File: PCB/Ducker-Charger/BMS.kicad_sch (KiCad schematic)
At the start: 0 parts

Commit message: feat: started BMS configuration
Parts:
- added C15, C16, C17, C18, C_VDD, C_VDD1: 1u, symbol Device:C
- added Q5, Q6: NCE3080K, EasyEDA:TO-252-2_L6.6-W6.1-P4.57-LS9.9-TL-CW, symbol EasyEDA:NCE3080K
- added R10: 10m, symbol Device:R
- added R11, R12, R13, R14, R15: 50, symbol Device:R
- added R_VDD: 1k, symbol Device:R
- added TH2: Thermistor_NTC, symbol Device:Thermistor_NTC
- added U4: BQ7791500PWR, EasyEDA:TSSOP-24_L7.8-W4.4-P0.65-LS6.4-BL, symbol EasyEDA:BQ7791500PWR
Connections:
- new net AVDD: C_VDD1.2, U4.2 (AVDD)
- new net BATT_+: R_VDD.1
- new net BATT_-: U4.9 (VSS)
- new net BATT_SENS_B+: R11.1
- new net BATT_SENS_B-: C_VDD.2, C_VDD1.1, R15.1
- new net BATT_SENS_B1: R14.1
- new net BATT_SENS_B2: R13.1
- new net BATT_SENS_B3: R12.1
- new net GND: U4.23 (CTRC), U4.24 (CTRD)
- new net VC0: C18.2, R15.2, U4.8 (VC0)
- new net VC1: C17.2, C18.1, R14.2, U4.7 (VC1)
- new net VC2: C16.2, C17.1, R13.2, U4.6 (VC2)
- new net VC3: C15.2, C16.1, R12.2, U4.5 (VC3)
- new net VC4: C15.1, R11.2, U4.3 (VC5), U4.4 (VC4)
- new net VDD: C_VDD.1, R_VDD.2, U4.1 (VDD)
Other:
- note added: "I_BAL = V_CELLA / (2 * R)=4.2V/100R=42mA P=RxI^2=~ 88mW"
- note added: "NB: VC5 and VC4 are shorted in order to make it usable with the configuration we are working with: 4s3p"
- note added: "NB: resistor package 0805, 0.125W"
- note added: "ntc need to be revaluated; i'd like to have at least 2 ntcs for parallel, but pheraps the distance will not allow it. i'm looking for a Epoxy NTC Thermistor with wire leads, which could be the answer to our problems"
- note added: "shunt"

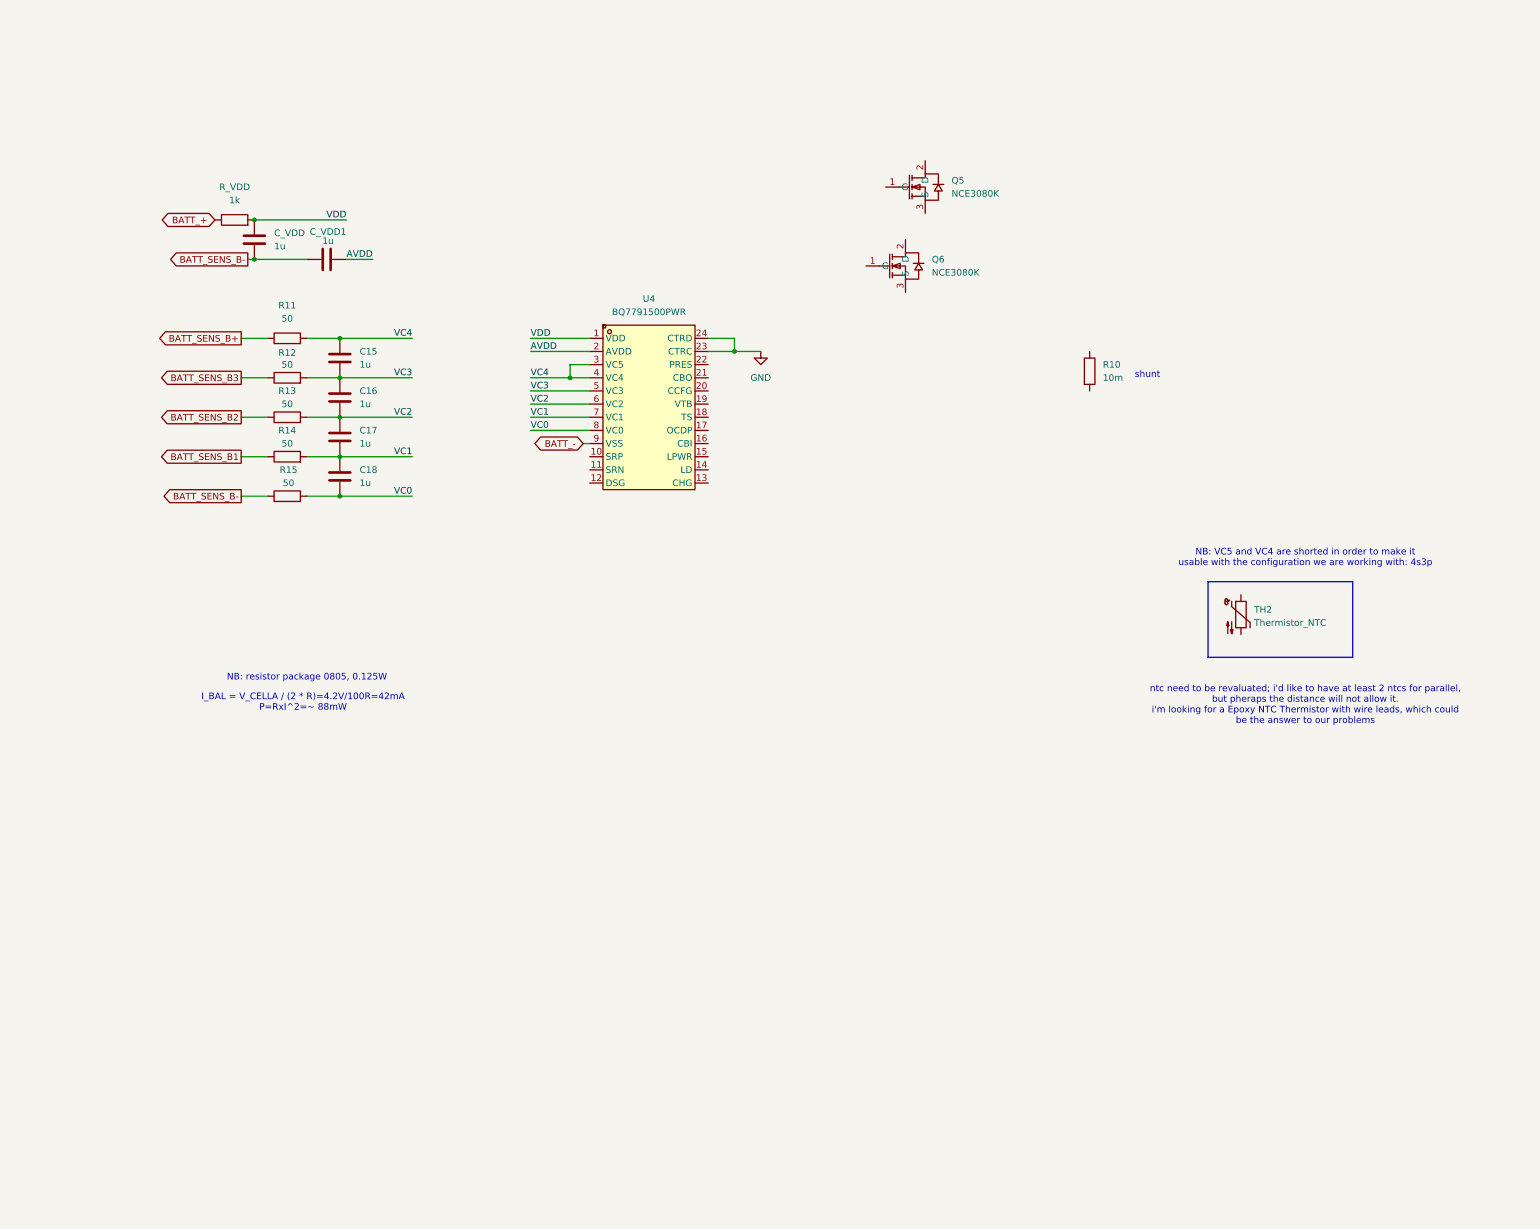
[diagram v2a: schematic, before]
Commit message: feat: started CHG and DSG in BMS
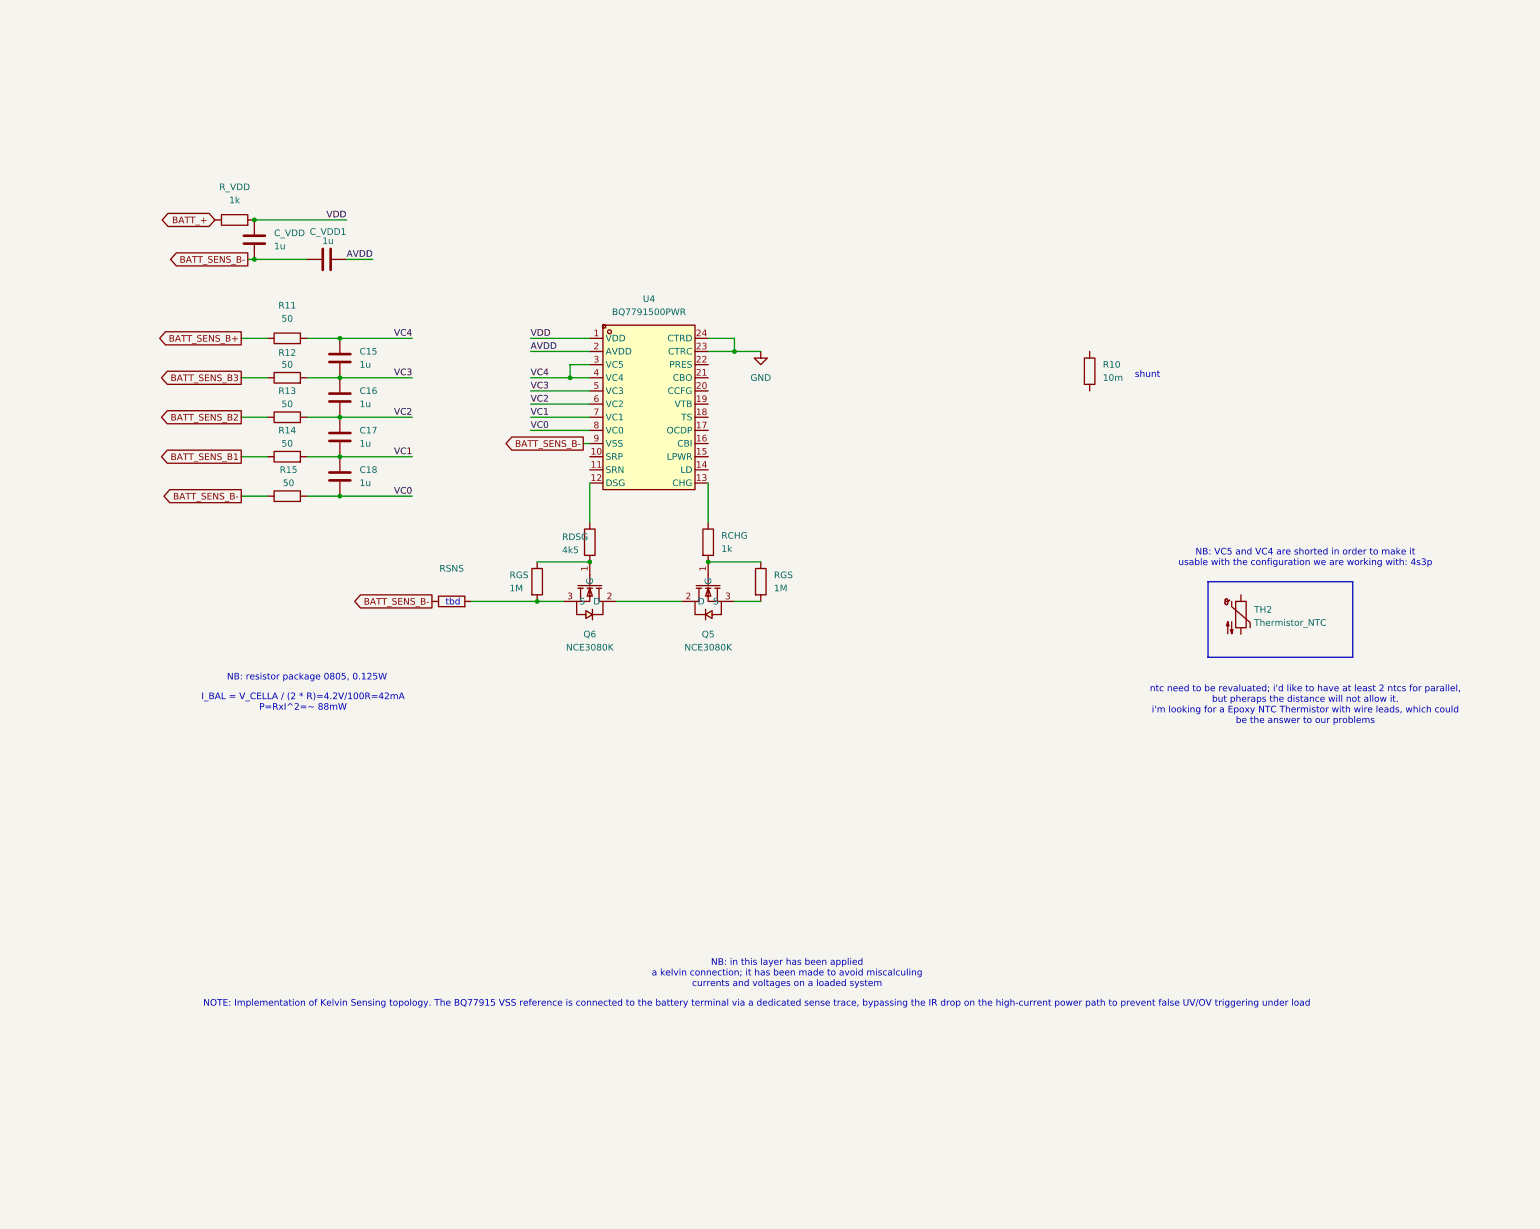
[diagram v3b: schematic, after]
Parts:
- added RCHG: 1k, symbol Device:R
- added RDSG: 4k5, symbol Device:R
- added RGS (x2): 1M, symbol Device:R
- added RSNS: ~, symbol Device:R
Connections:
- net BATT_- is gone; now on net BATT_SENS_B-: U4.9 (VSS)
- net BATT_SENS_B-: now also RSNS.1
- net at U4.12 (DSG): now also RDSG.1
- net at U4.13 (CHG): now also RCHG.1
- net at Q5.1 (G): now also RCHG.2, RGS.1
- net at Q5.2 (D): now also Q6.2 (D)
- net at Q5.3 (S): now also RGS.2
- net at Q6.1 (G): now also RDSG.2, RGS.1
- net at Q6.3 (S): now also RGS.2, RSNS.2
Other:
- note added: "NB: in this layer has been applied a kelvin connection; it has been made to avoid miscalculing currents and voltages on a loaded system"
- note added: "NOTE: Implementation of Kelvin Sensing topology. The BQ77915 VSS reference is connected to the battery terminal via a dedicated sense trace, bypassing the IR drop on the high-current power path to prevent false UV/OV triggering under load"
- note added: "tbd"
- moved on the sheet: Q5, Q6

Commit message: feat: implement basic BQ77915 protection circuit
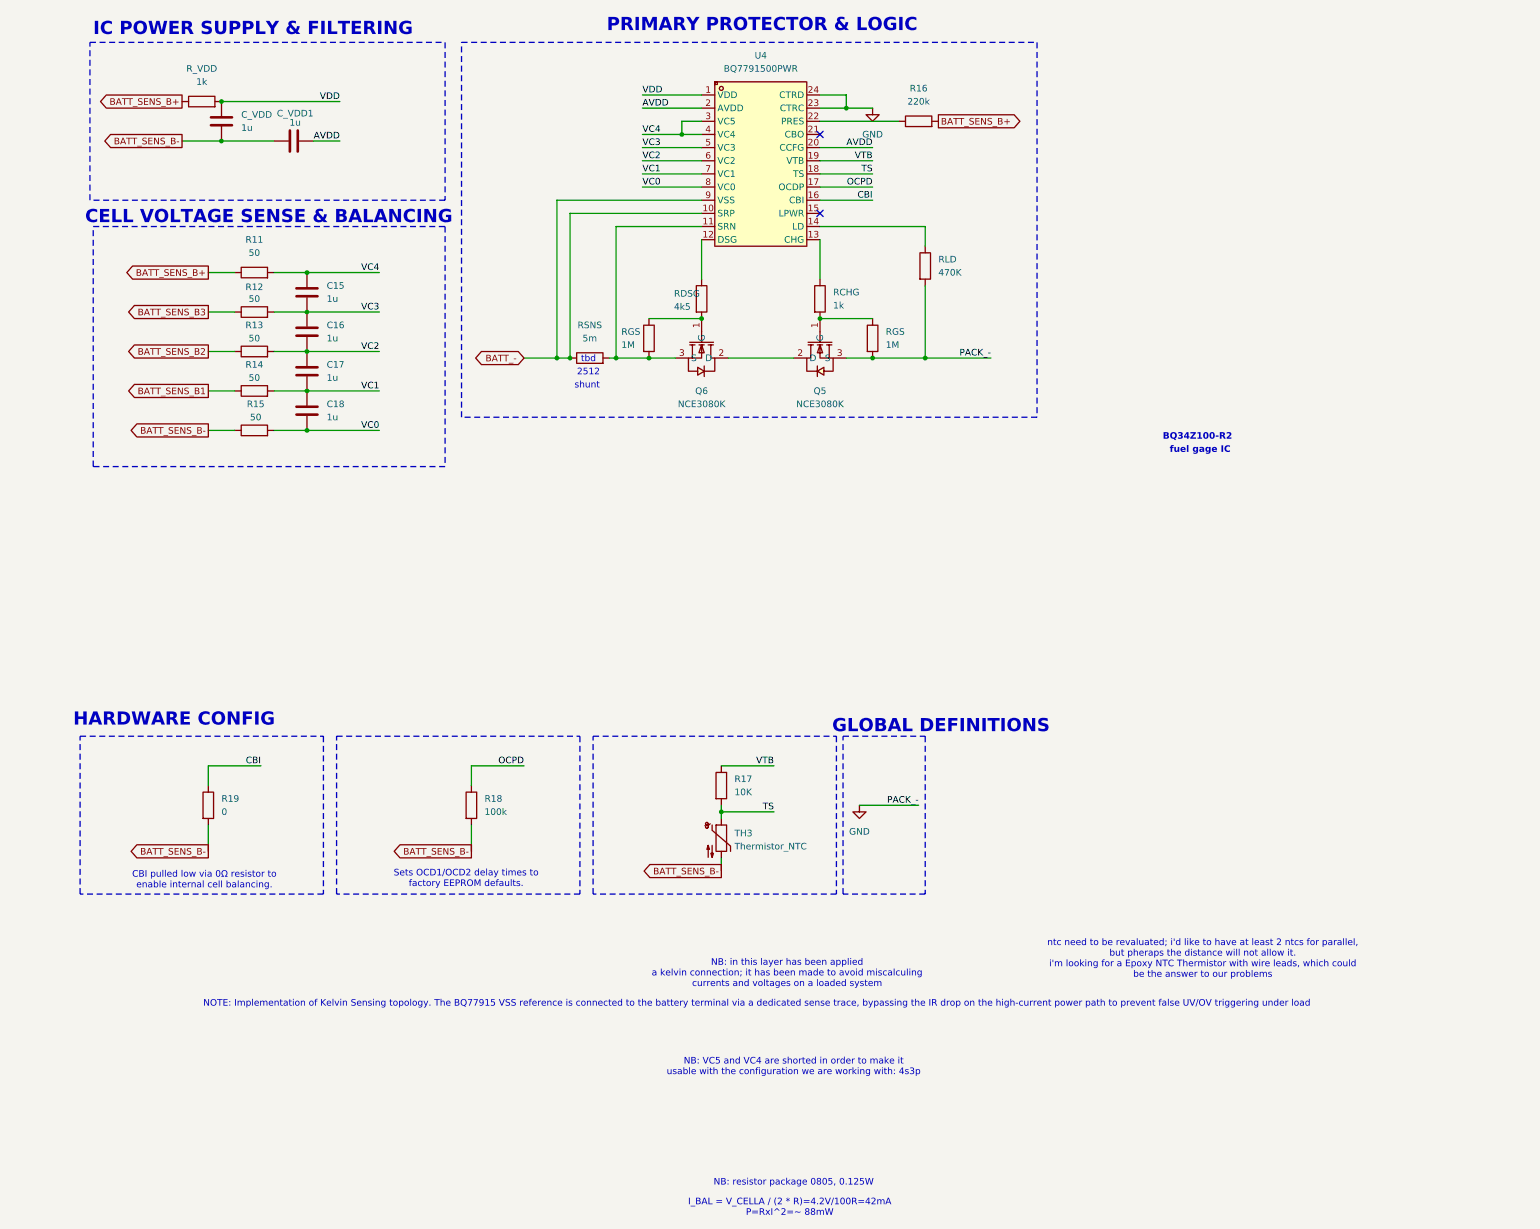
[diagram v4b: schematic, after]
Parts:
- removed R10: 10m, symbol Device:R
- removed TH2: Thermistor_NTC, symbol Device:Thermistor_NTC
- added R16: 220k, symbol Device:R
- added R17: 10K, symbol Device:R
- added R18: 100k, symbol Device:R
- added R19: 0, symbol Device:R
- added RLD: 470K, symbol Device:R
- added TH3: Thermistor_NTC, symbol Device:Thermistor_NTC
- RSNS: value ~ -> 5m; lcsc name (none) -> Milliohm HoJLR2512-3W-5mR-1%
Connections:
- net BATT_+ is gone; now on net BATT_SENS_B+: R_VDD.1
- net AVDD: now also U4.20 (CCFG)
- net BATT_SENS_B+: now also R16.2
- net BATT_SENS_B-: now also R18.2, R19.2, TH3.2; no longer RSNS.1, U4.9 (VSS)
- net GND: now also Q5.3 (S), RGS.2, RLD.2
- net at Q6.3 (S), RGS.2, RSNS.2: now also U4.11 (SRN)
- net BATT_-: now reaches U4.10 (SRP)
- net BATT_-: now also RSNS.1, U4.9 (VSS)
- net at U4.14 (LD): now also RLD.1
- net CBI: now reaches U4.16 (CBI)
- net CBI: now also R19.1
- net OCPD: now reaches U4.17 (OCDP)
- net OCPD: now also R18.1
- net TS: now reaches U4.18 (TS)
- net TS: now also R17.2, TH3.1
- net VTB: now reaches U4.19 (VTB)
- net VTB: now also R17.1
- net at U4.22 (PRES): now also R16.1
- no-connect marks 0 -> 2
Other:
- note added: "2512"
- note added: "BQ34Z100-R2"
- note added: "CBI pulled low via 0Ω resistor to enable internal cell balancing."
- note added: "CELL VOLTAGE SENSE & BALANCING"
- note added: "GLOBAL DEFINITIONS"
- note added: "HARDWARE CONFIG"
- note added: "IC POWER SUPPLY & FILTERING"
- note added: "PRIMARY PROTECTOR & LOGIC"
- note added: "Sets OCD1/OCD2 delay times to factory EEPROM defaults."
- note added: "fuel gage IC"
- moved on the sheet: C15, C16, C17, C18, C_VDD, C_VDD1, Q5, Q6, R11, R12, R13, R14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
